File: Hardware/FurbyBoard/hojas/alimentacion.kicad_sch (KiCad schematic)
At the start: 34 parts, among them J2 BAT+, J3 BAT-, Q1 SI7615ADN, U2 BQ24073RGTR, U3 TPS63802DLAR

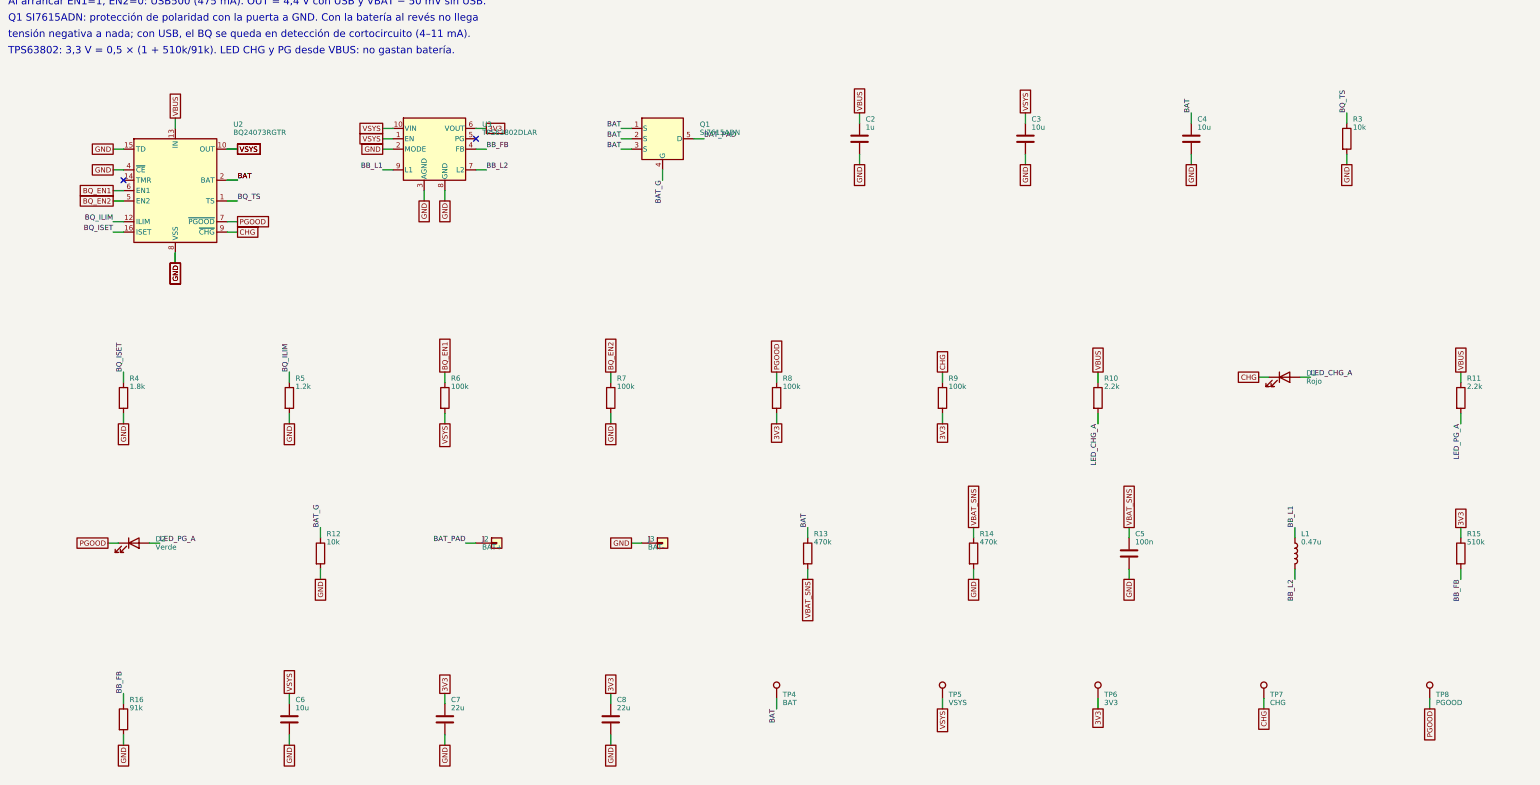
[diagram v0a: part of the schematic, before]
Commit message: Refactor: pads de cable agrupados por zona y etiquetas globales
- Motor en J9 con leva, encoder y sensores; altavoz en J8 con inclinación y
  lengua; luz en J7 con el IR. Desaparecen J4 y J10: cada grupo sale por el
  borde más cercano a su destino.
- Micro en 2x03 en vez de 1x06 para que quepa junto al borde derecho.
- Todas las etiquetas del esquemático son globales, así el nombre de red
  coincide con el del PCB (paridad sin prefijos de hoja).
- ERC 0 errores, 0 avisos.

Co-Authored-By: Claude Opus 5.5 (1M context) <noreply@anthropic.com>
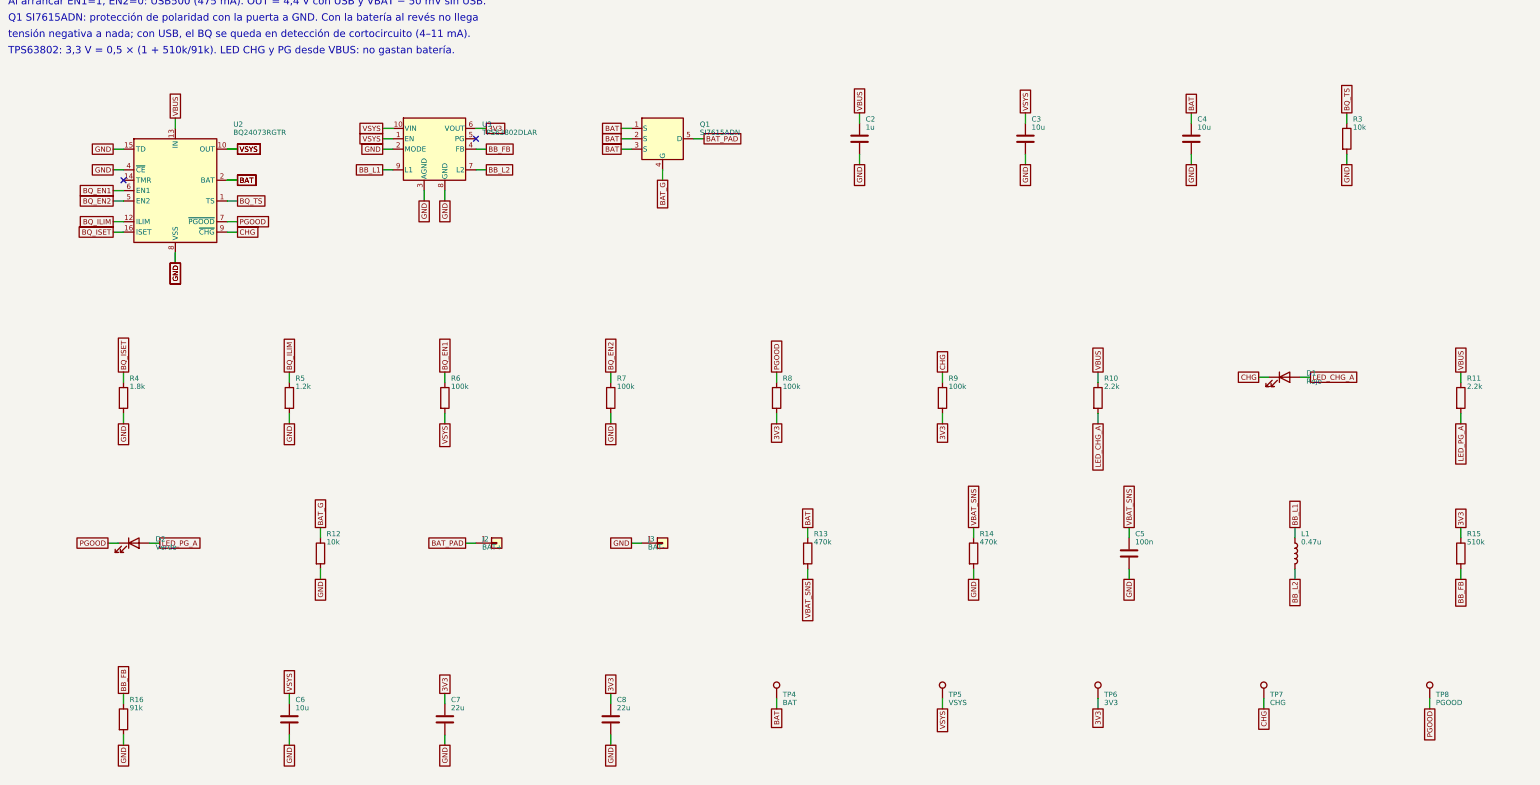
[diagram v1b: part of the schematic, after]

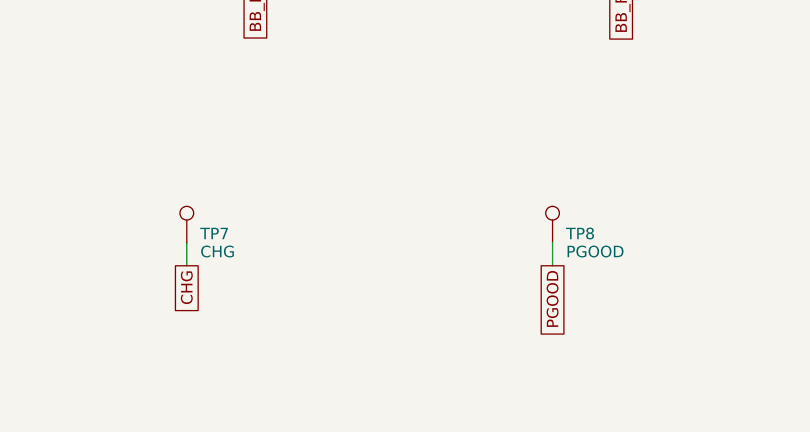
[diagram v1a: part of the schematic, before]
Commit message: Feature: par USB trazado, planos GND/VSYS y serigrafía de la FurbyBoard
- Par USB de J1 al ESD y al módulo, acoplado 0,28/0,15 por F.Cu sobre el
  plano de GND, sin vías (rutas_fijas.py, bloqueado para el autorrutado).
  Canal libre en x -83 bajo la batería.
- In1 plano de GND e In2 plano de VSYS; potencia por pista a 0,4 (cabe en
  los pads de 0,5 de paso) y 3V3 a 0,3. exportar_dsn.py deja el DSN para
  Freerouting con las clases de red.
- Rótulos de serigrafía colocados solos (serigrafia.py): TP, LED, botones,
  puentes y polaridad de la batería arriba; función de cada pad de cable y
  GPIO del J_EXP abajo, con leyenda para J7, J9 y J5.
- Para que quepan los rótulos: fila de LED con resistencias debajo, botones
  en vertical, rejilla de TP con el rótulo debajo. Quedan 14 TP: fuera EN e
  IO0 (se miden en los pads de SW1 y SW2), CHG y PG (en D1 y D2) y un GND.

ERC 0/0. DRC 0 salvo una vía de GND sin plano relleno; sin rutar.

Co-Authored-By: Claude Opus 5.5 (1M context) <noreply@anthropic.com>
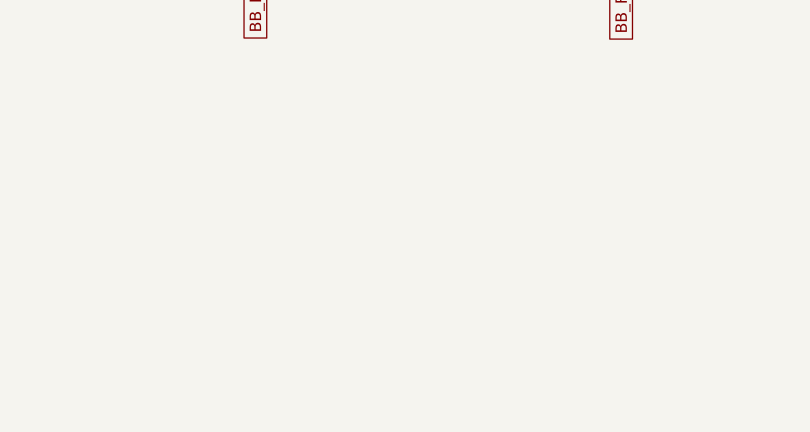
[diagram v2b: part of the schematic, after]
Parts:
- removed TP7: CHG, TestPoint:TestPoint_Pad_D1.5mm, symbol Connector:TestPoint
- removed TP8: PGOOD, TestPoint:TestPoint_Pad_D1.5mm, symbol Connector:TestPoint

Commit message: Feature: esquema de la FurbyBoard al procedimiento nuevo: rúbrica L, reglas por red, pines por geometría y simulación del elevador
- Rúbrica S/M/L (L) y tabla de raíles con anchos mínimos (params.ANCHOS_MINIMOS), que gen_pro.py vuelca al .kicad_dru como una regla por red, con cuellos dentro de los patios de los QFN y de J1.
- Vías de 0,45/0,2 solo en la clase USB (cruce del par en el receptáculo de 16 pines); el resto sigue en 0,6/0,3.
- pcb-toolkit.toml: clases B/C/D, anchos, grupos explícitos y zonas del puente H y de la clase D.
- Redes a la convención: BB_SW1/2, I2S_SCK_MIC/I2S_WS_MIC.
- Pines del módulo (I2S, HOME, EXP_INT) y puertos del TCA9535 por geometría, sin tocar strapping, USB ni ADC.
- LED del encoder desde V6 por 470 ohm (sin Q2); J_EXP 2x5; J9 y J5 reordenados; serigrafía al día.
- ERC 0/0. Simulación ngspice del elevador en el peor caso (sim/). Informes de las puertas A y B en revisiones/; un crítico (NTC del cargador) queda escalado.

Co-Authored-By: Claude Fable 5.1 <noreply@anthropic.com>
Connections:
- net BB_L1 renamed BB_SW1
- net BB_L2 renamed BB_SW2
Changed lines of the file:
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@@
 		)
 	)
-	(global_label "BB_L1"
+	(global_label "BB_SW1"
 		(shape passive)
 		(at 335.28 163.83 90)
@@
 		)
 	)
-	(global_label "BB_L2"
+	(global_label "BB_SW2"
 		(shape passive)
 		(at 137.16 76.2 0)
@@
 		)
 	)
-	(global_label "BB_L2"
+	(global_label "BB_SW2"
 		(shape passive)
 		(at 335.28 176.53 270)
@@
 		)
 	)
-	(global_label "BB_L1"
+	(global_label "BB_SW1"
 		(shape passive)
 		(at 111.76 76.2 180)

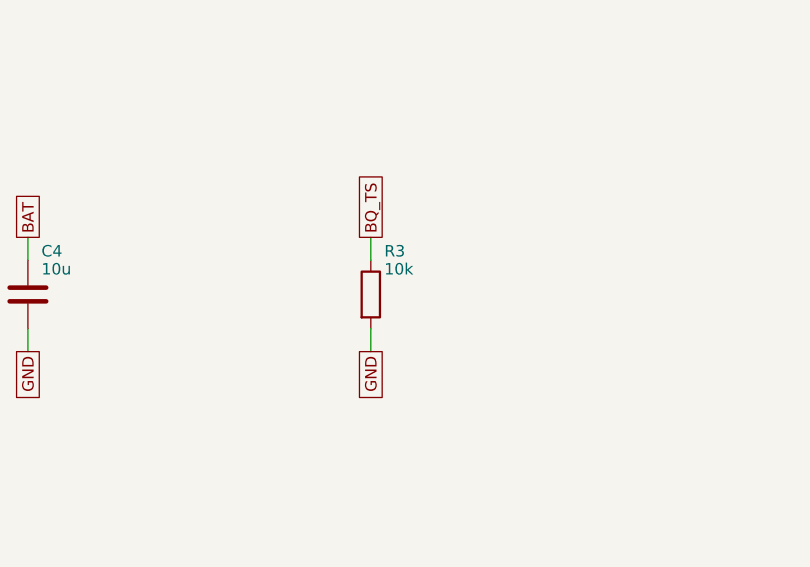
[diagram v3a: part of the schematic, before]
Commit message: Feature: NTC de 10 kΩ en TS del cargador (R4) y BQ_TS como red crítica
RT1 Murata NCP18XH103F03RB (C13564) de TS a VSS como pide el BQ2407x,
sin red de polarización; la red BQ_TS entra en las críticas de
pcb-toolkit.toml. ERC 0 infracciones.

Co-Authored-By: Claude Fable 5.1 <noreply@anthropic.com>
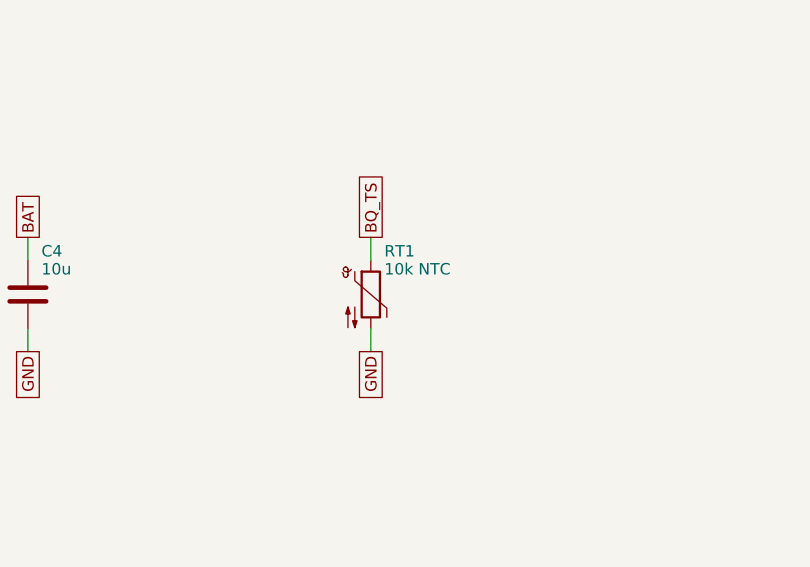
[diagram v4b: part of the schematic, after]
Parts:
- removed R3: 10k, Resistor_SMD:R_0603_1608Metric, symbol Device:R
- added RT1: 10k NTC, Resistor_SMD:R_0603_1608Metric, symbol Device:Thermistor_NTC
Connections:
- net BQ_TS: now also RT1.1
- net GND: now also RT1.2
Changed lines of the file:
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@@
 	)
 	(symbol
-		(lib_id "Device:R")
+		(lib_id "Device:Thermistor_NTC")
 		(at 347.98 68.58 0)
 		(unit 1)
@@
 		(in_pos_files yes)
 		(dnp no)
-		(property "Reference" "R3"
+		(property "Reference" "RT1"
 			(at 349.48 63.77 0)
 			(show_name no)
@@
 			)
 		)
-		(property "Value" "10k"
+		(property "Value" "10k NTC"
 			(at 349.48 65.77 0)
 			(show_name no)
@@
 			)
 		)
-		(property "Description" "TS sin NTC"
+		(property "Description" "NTC 10 kΩ B3380 0603 en TS (carga 0–45 °C)"
 			(at 347.98 68.58 0)
 			(hide yes)
@@
 			)
 		)
-		(property "LCSC" "C25804"
+		(property "LCSC" "C13564"
 			(at 347.98 68.58 0)
 			(hide yes)
@@
 			)
 		)
-		(property "JLC_Class" "base"
+		(property "JLC_Class" "ext"
 			(at 347.98 68.58 0)
 			(hide yes)
@@
 			)
 		)
-		(property "MPN" "UNI-ROYAL 0603 1%"
+		(property "MPN" "Murata NCP18XH103F03RB"
 			(at 347.98 68.58 0)
 			(hide yes)
@@
 			(project "FurbyBoard"
 				(path "/8b4f1e2a-3c5d-4e6f-9a1b-2c3d4e5f6a7b/f3e50cc9-b269-5cfc-8a97-7683b547d39e"
-					(reference "R3")
+					(reference "RT1")
 					(unit 1)
 				)
